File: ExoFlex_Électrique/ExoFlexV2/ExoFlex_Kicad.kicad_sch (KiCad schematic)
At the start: 25 parts, among them J1 ScrewT+12V, J19 CN9, J2 ScrewT5V, J20 CN10, J3 ScrewTGND, J4 ScrewT12V, J5 ScrewT-12v, J6 CN7, J7 CN8, M1 MOT_EV(12V 9.2A), M2 MOT_DOR(12V 9.2A), P1 Conn_WallPlug, U2 ON/OFF_SW(20A), U3 SECU_BUT(20A)

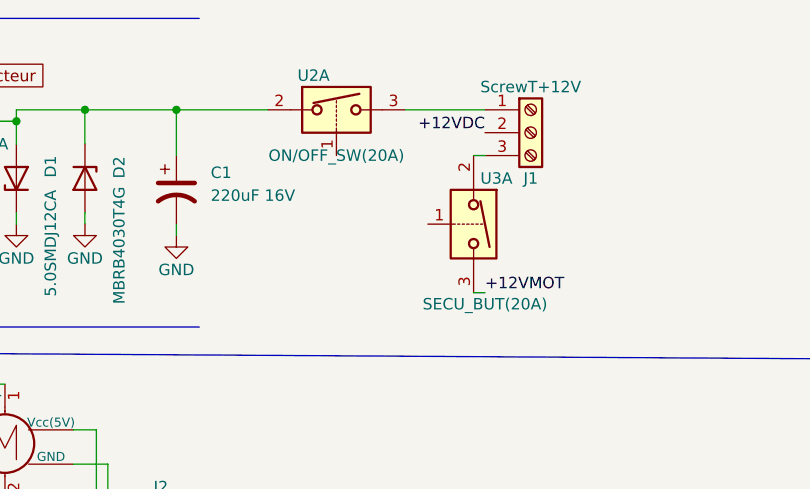
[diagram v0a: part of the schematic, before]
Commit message: Ajout outline
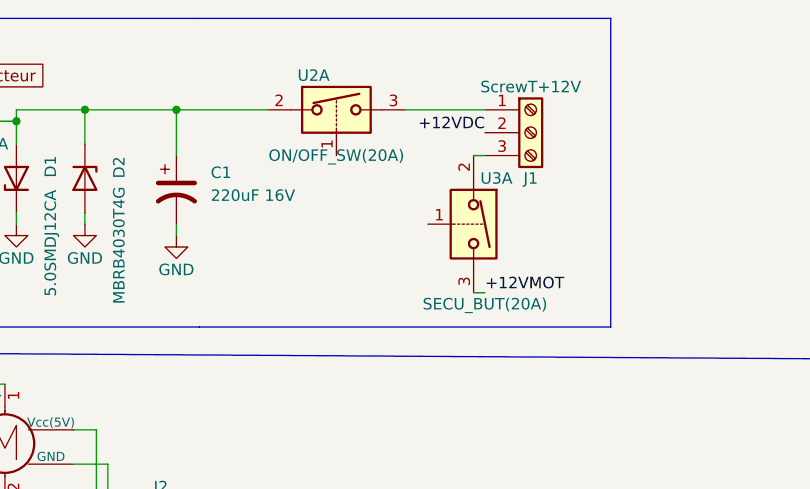
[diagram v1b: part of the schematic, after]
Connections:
- net at PS1.3 (-Vout): now also J5.1 (Pin_1)
- net at PS1.4 (+Vout): now also FL1.4
- net at P?.S1 (Data_1): now also U?.3
- net at P?.S2 (Data_2): now also PS?.4 (-Vout)
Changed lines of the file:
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@@
+    (stroke (width 0) (type default) (color 0 0 0 0))
+  )
+  (polyline (pts (xy 168.91 15.24) (xy 214.63 15.24))
     (stroke (width 0) (type default) (color 0 0 0 0))
   )
@@
     (stroke (width 0) (type default) (color 0 0 0 0))
   )
+  (polyline (pts (xy 168.91 49.53) (xy 214.63 49.53))
+    (stroke (width 0) (type default) (color 0 0 0 0))
+  )
   (wire (pts (xy 116.84 21.59) (xy 119.38 21.59))
     (stroke (width 0) (type default) (color 0 0 0 0))
@@
     (stroke (width 0) (type default) (color 0 0 0 0))
   )
+  (polyline (pts (xy 214.63 49.53) (xy 214.63 15.24))
+    (stroke (width 0) (type default) (color 0 0 0 0))
+  )

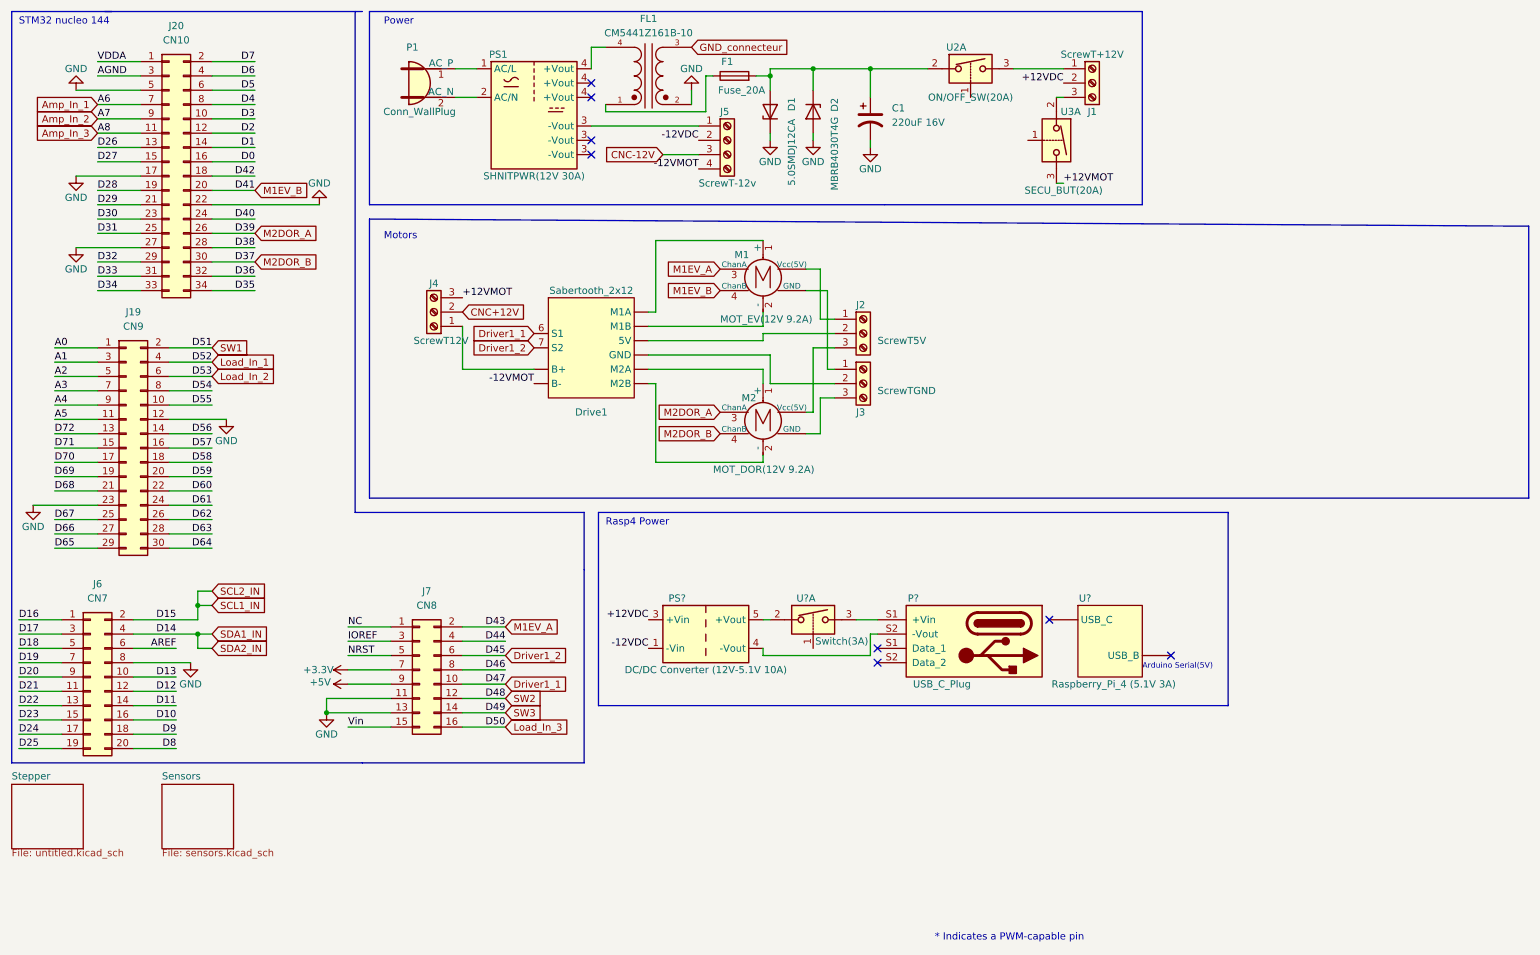
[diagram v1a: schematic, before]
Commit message: Modification du schéma électrique en enlevant les cellules de charge et les cicuits de potentio
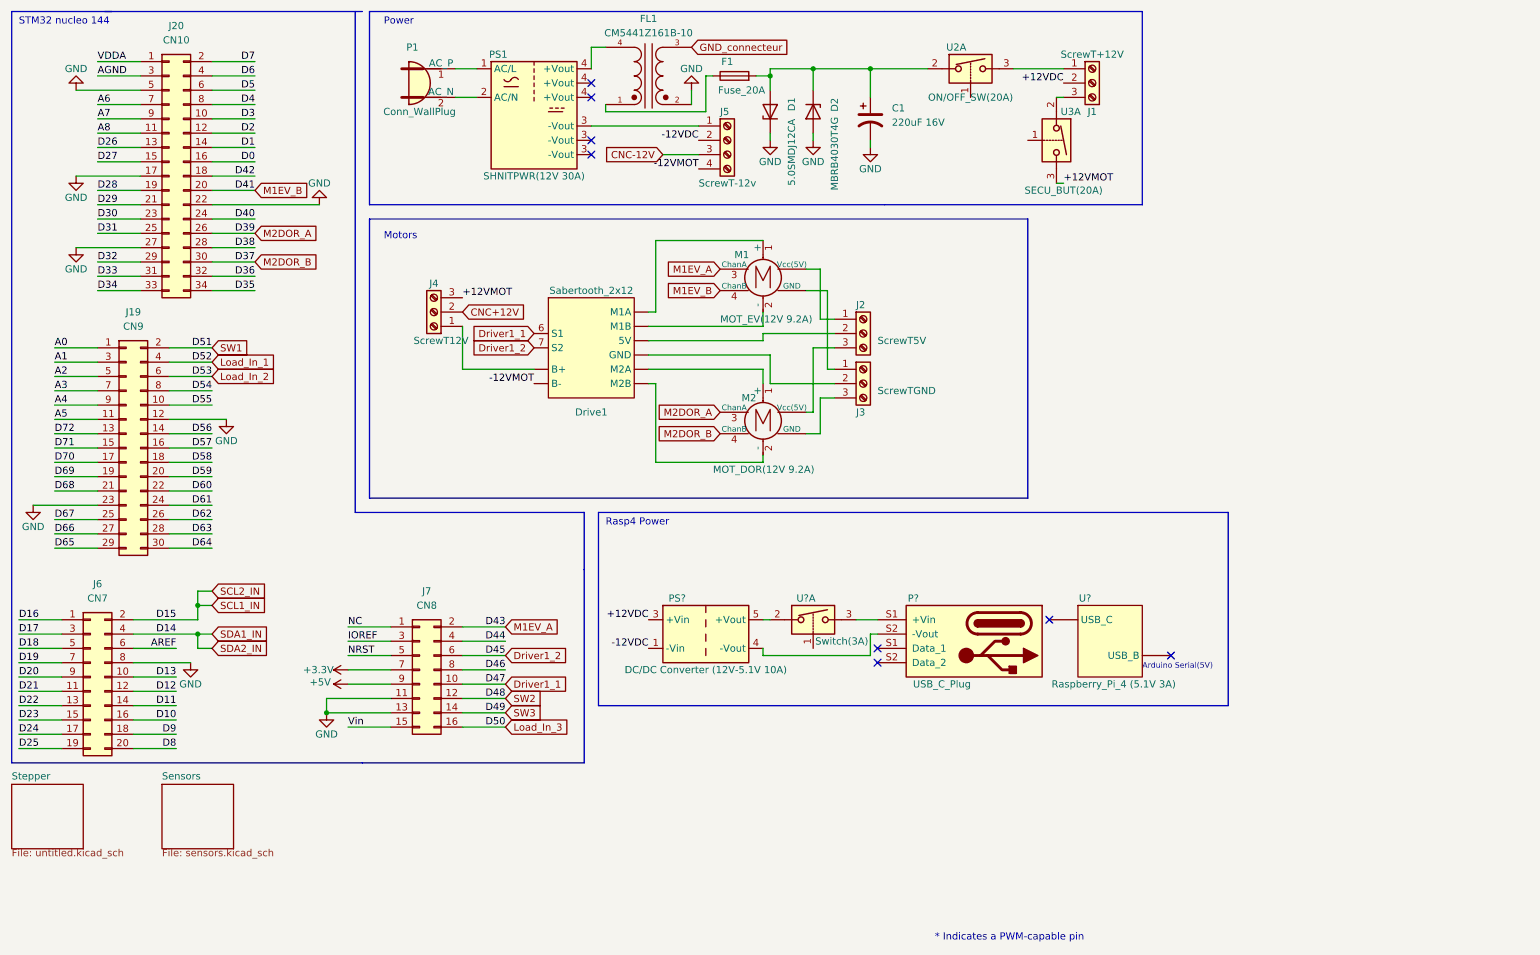
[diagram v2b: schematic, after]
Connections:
- net at PS1.3 (-Vout): now also J5.1 (Pin_1)
- net at PS1.4 (+Vout): now also FL1.4
- net at P?.S1 (Data_1): now also U?.3
- net at P?.S2 (Data_2): now also PS?.4 (-Vout)
- net Amp_In_1 renamed A6
- net Amp_In_2 renamed A7
- net Amp_In_3 renamed A8
